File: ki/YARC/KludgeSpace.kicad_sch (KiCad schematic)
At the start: 5 parts, among them J8 6-PIN FROM MCR, U100 74LS32, U101 74LS157, U139 74HC74, U140 74LS32

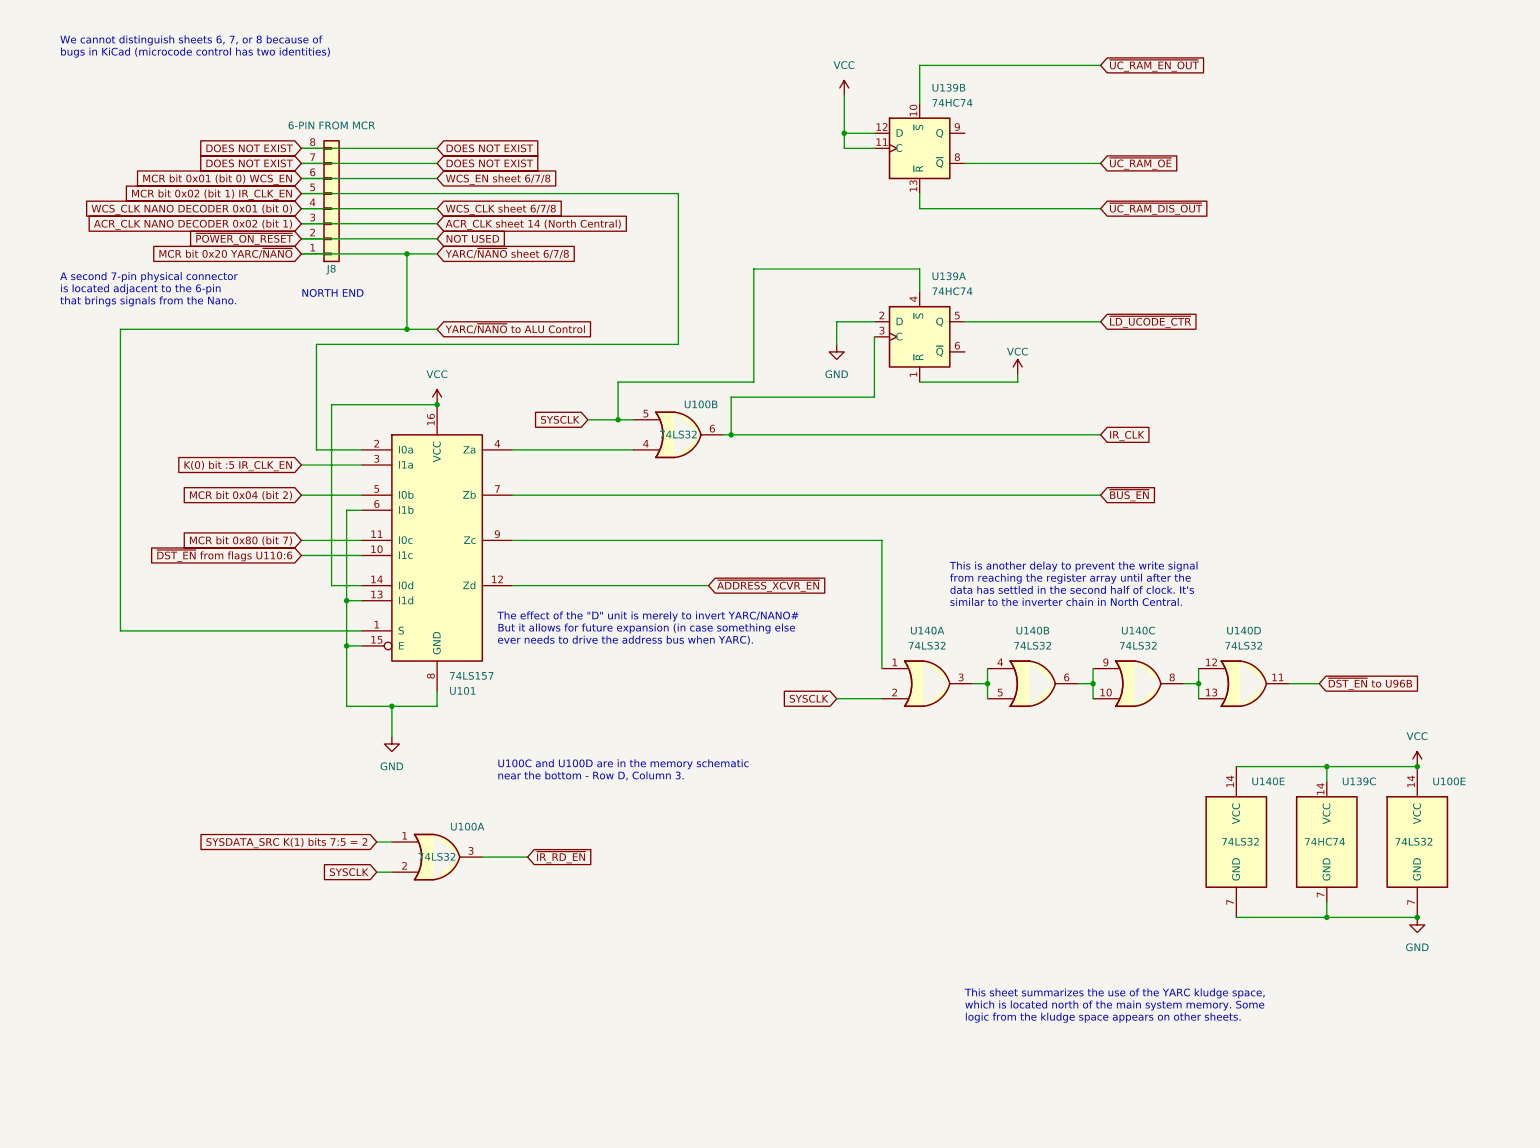
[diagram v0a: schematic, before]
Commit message: Ongoing fixes for ERC errors
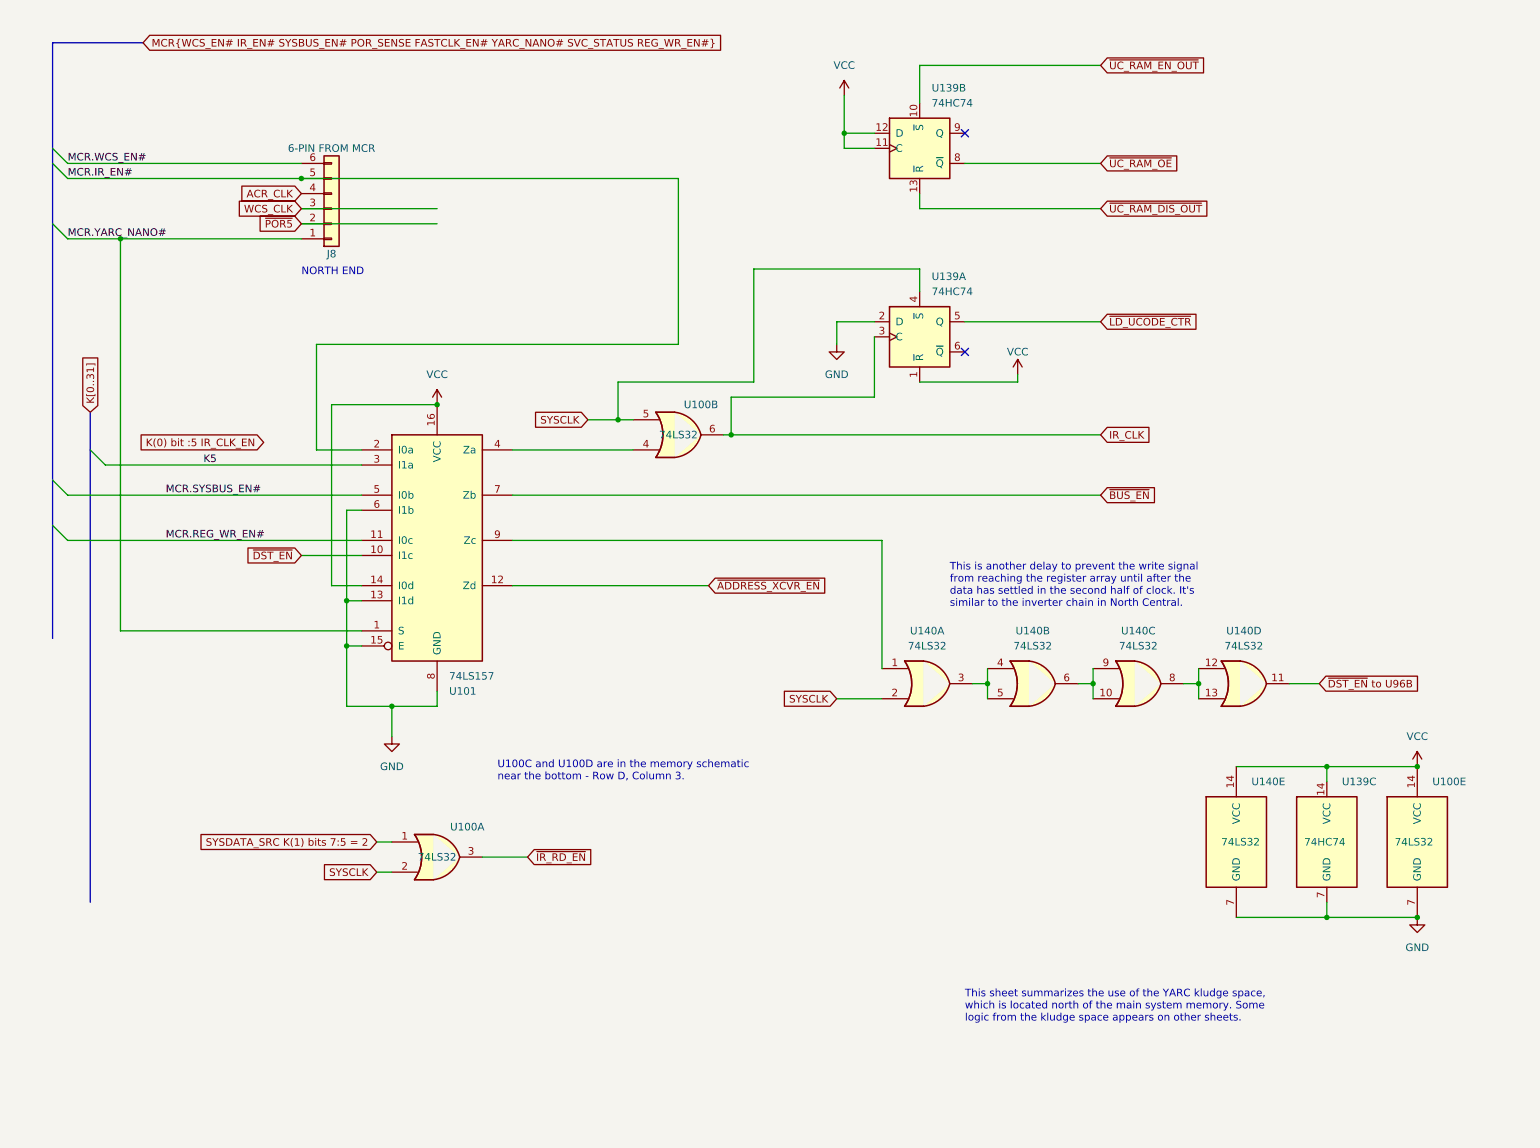
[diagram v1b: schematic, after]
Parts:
- J8: symbol Connector_Generic:Conn_01x08 -> Connector_Generic:Conn_01x06
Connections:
- net K(0) bit :5 IR_CLK_EN: no longer U101.3 (I1a)
- net ACR_CLK NANO DECODER 0x02 (bit 1) renamed WCS_CLK
- removed net DOES NOT EXIST: J8.7 (Pin_7), J8.8 (Pin_8)
- net MCR bit 0x01 (bit 0) WCS_EN renamed MCR.WCS_EN#
- net MCR bit 0x02 (bit 1) IR_CLK_EN renamed MCR.IR_EN#
- net MCR bit 0x04 (bit 2) renamed MCR.SYSBUS_EN#
- net MCR bit 0x20 YARC/~{NANO} renamed MCR.YARC_NANO#
- net MCR bit 0x80 (bit 7) renamed MCR.REG_WR_EN#
- net NOT USED renamed ~{POR5}
- net WCS_CLK NANO DECODER 0x01 (bit 0) renamed ACR_CLK
- net ~{DST_EN} from flags U110:6 renamed ~{DST_EN}
- new net K5: U101.3 (I1a)
- no-connect marks 0 -> 2
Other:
- note removed: "A second 7-pin physical connector is located adjacent to the 6-pin that brings signals from the Nano."
- note removed: "The effect of the "D" unit is merely to invert YARC/NANO# But it allows for future expansion (in case something else ever needs to drive the address bus when YARC)."
- note removed: "We cannot distinguish sheets 6, 7, or 8 because of bugs in KiCad (microcode control has two identities)"

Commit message: Ongoing schematic changes
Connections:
- net SYSDATA_SRC K(1) bits 7:5 = 2 renamed ~{SYSDATA_SRC_IS_IR}
- net ~{ADDRESS_XCVR_EN} renamed ~{GRtoA}
- net ~{DST_EN} to U96B renamed ~{DST_EN_DLY}
- net ~{IR_RD_EN} renamed ~{IR_RD}
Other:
- note added: "Delay the load of the microcode counter by 1/2 clock."
- note added: "Delay to prevent the write signal from reaching the register array until after the data has settled in the second half of clock. Similar to the inverter chain in North Central."
- note added: "Enable data output from the microcode RAMs from the Nano's pulse outputs."
- note added: "To U96B on p.10, GeneralRegisters"
- note added: "U100C and U100D are on the memory schematic."
- note removed: "This is another delay to prevent the write signal from reaching the register array until after the data has settled in the second half of clock. It's similar to the inverter chain in North Central."
- note removed: "U100C and U100D are in the memory schematic near the bottom - Row D, Column 3."
- moved on the sheet: J8, U100A, U100E, U101, U139A, U139B, U139C, U140A, U140B, U140C, U140D, U140E

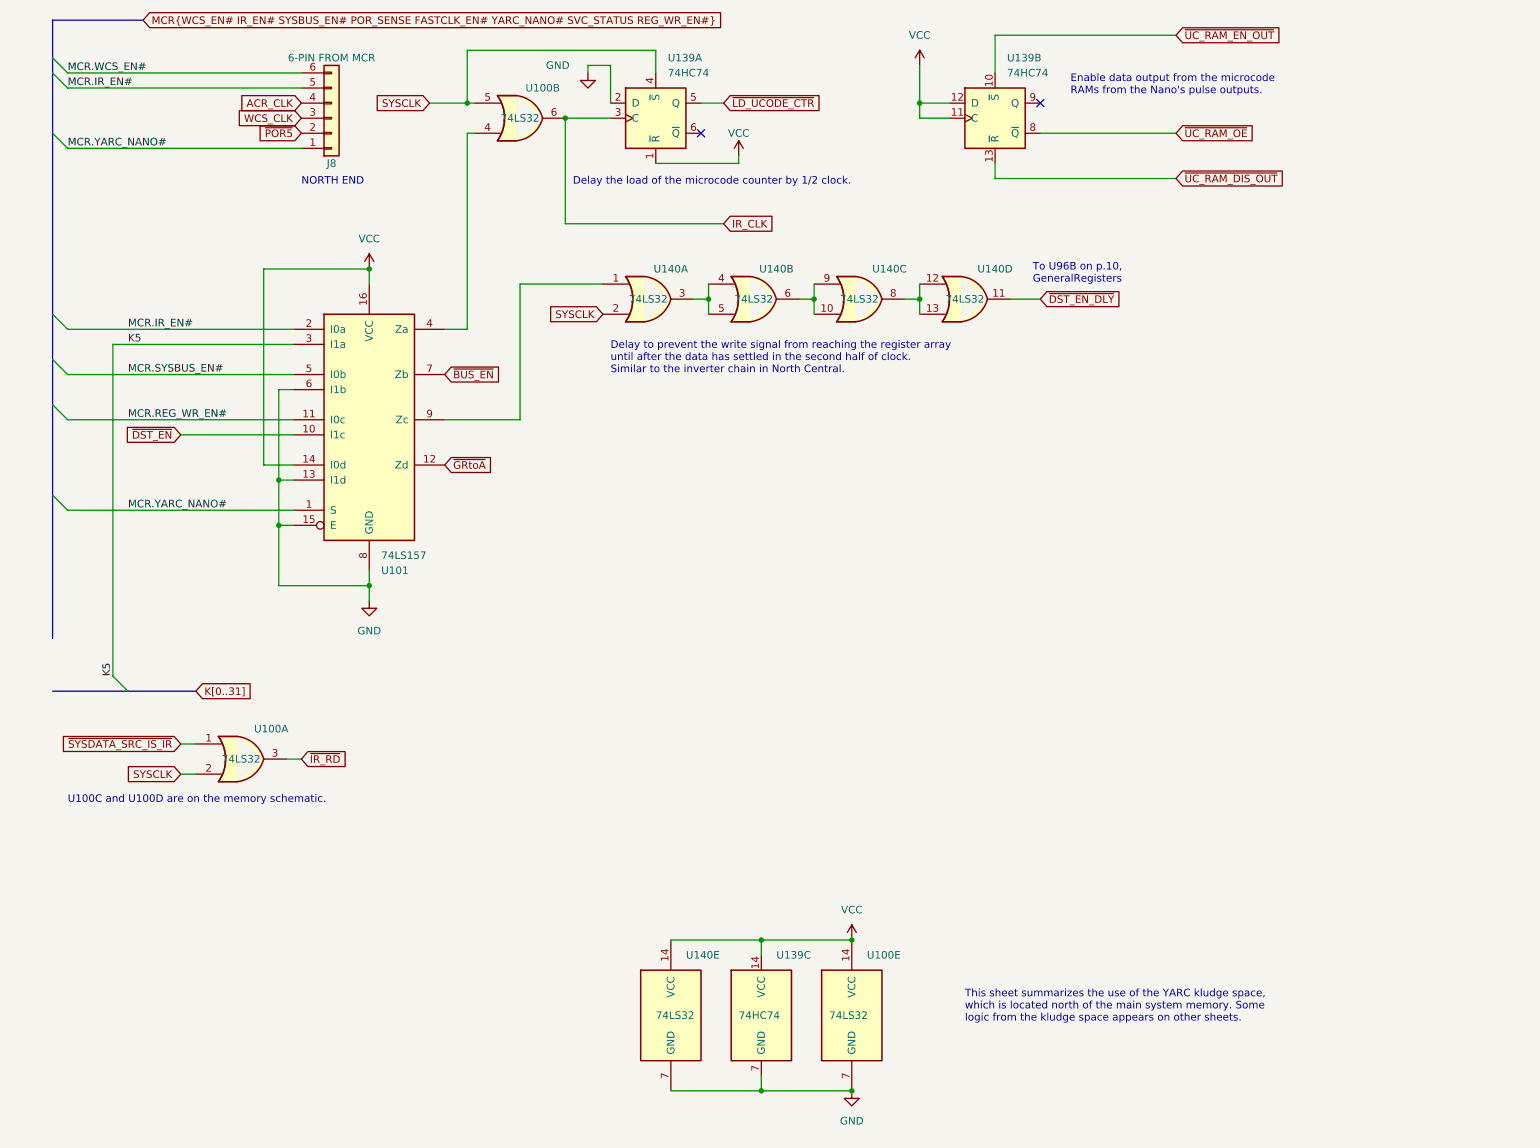
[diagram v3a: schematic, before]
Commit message: Schematic for addressing unit is complete and all ERC violations addressed
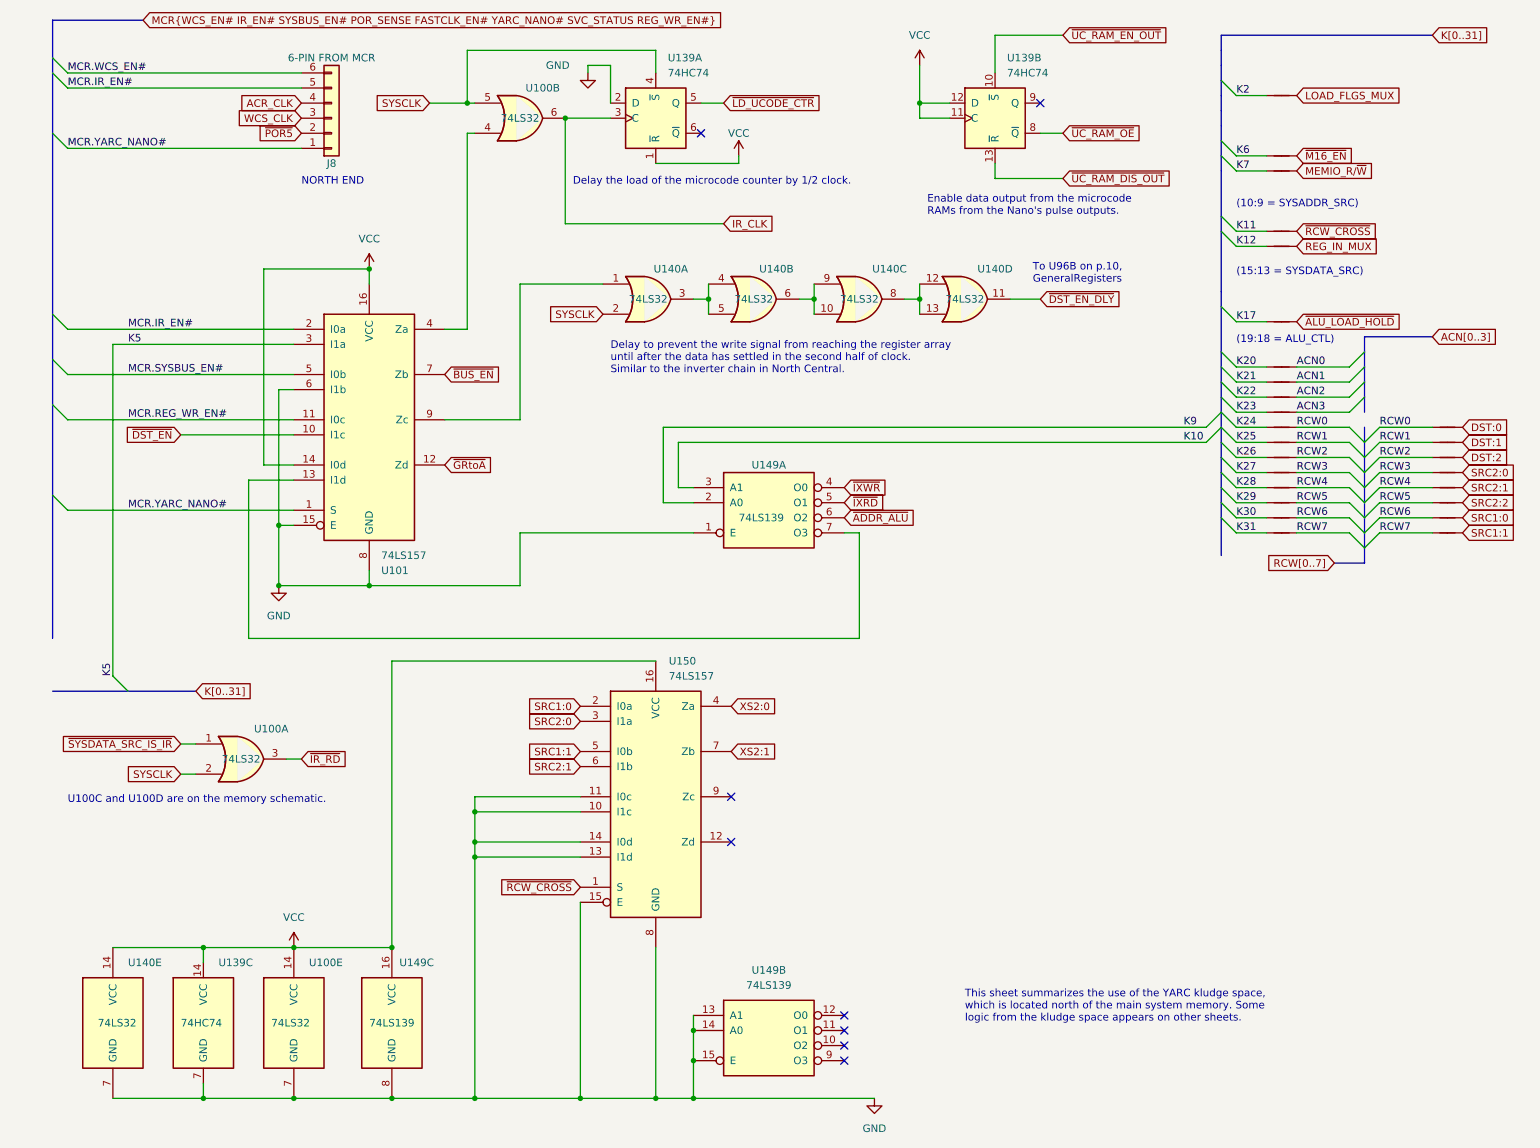
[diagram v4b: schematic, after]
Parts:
- added NT148, NT152, NT153, NT157, NT158, NT163, NT166, NT167, NT168, NT169, NT170, NT171, NT172, NT173, NT174, NT175, NT176, NT177, NT178, NT179, NT180, NT181, NT182, NT183, NT184, NT185: NetTie_2, symbol Device:NetTie_2
- added U149: 74LS139, symbol 74xx:74LS139
- added U150: 74LS157, symbol 74xx:74LS157
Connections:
- net GND: now also U149.1 (E), U149.13 (A1), U149.14 (A0), U149.15 (E), U149.8 (GND), U150.10 (I1c), U150.11 (I0c), U150.13 (I1d), U150.14 (I0d), U150.15 (E), U150.8 (GND); no longer U101.13 (I1d)
- net VCC: now also U149.16 (VCC), U150.16 (VCC)
- new net: U101.13 (I1d), U149.7 (O3)
- new net ACN0: NT166.2
- new net ACN1: NT167.2
- new net ACN2: NT168.2
- new net ACN3: NT169.2
- new net DST:0: NT178.2
- new net DST:1: NT179.2
- new net DST:2: NT180.2
- new net K10: U149.3 (A1)
- new net K11: NT157.1
- new net K12: NT158.1
- new net K17: NT163.1
- new net K2: NT148.1
- new net K20: NT166.1
- new net K21: NT167.1
- new net K22: NT168.1
- new net K23: NT169.1
- new net K24: NT170.1
- new net K25: NT171.1
- new net K26: NT172.1
- new net K27: NT173.1
- new net K28: NT174.1
- new net K29: NT175.1
- new net K30: NT176.1
- new net K31: NT177.1
- new net K6: NT152.1
- new net K7: NT153.1
- new net K9: U149.2 (A0)
- new net LOAD_FLGS_MUX: NT148.2
- new net MEMIO_R/~{W}: NT153.2
- new net RCW0: NT170.2, NT178.1
- new net RCW1: NT171.2, NT179.1
- new net RCW2: NT172.2, NT180.1
- new net RCW3: NT173.2, NT181.1
- new net RCW4: NT174.2, NT182.1
- new net RCW5: NT175.2, NT183.1
- new net RCW6: NT176.2, NT184.1
- new net RCW7: NT177.2, NT185.1
- new net REG_IN_MUX: NT158.2
- new net SRC1:0: NT184.2, U150.2 (I0a)
- new net SRC1:1: NT185.2, U150.5 (I0b)
- new net SRC2:0: NT181.2, U150.3 (I1a)
- new net SRC2:1: NT182.2, U150.6 (I1b)
- new net SRC2:2: NT183.2
- new net XS2:0: U150.4 (Za)
- new net XS2:1: U150.7 (Zb)
- new net ~{ADDR_ALU}: U149.6 (O2)
- new net ~{ALU_LOAD_HOLD}: NT163.2
- new net ~{IXRD}: U149.5 (O1)
- new net ~{IXWR}: U149.4 (O0)
- new net ~{M16_EN}: NT152.2
- new net ~{RCW_CROSS}: NT157.2, U150.1 (S)
- no-connect marks 2 -> 8
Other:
- note added: "(10:9 = SYSADDR_SRC)"
- note added: "(15:13 = SYSDATA_SRC)"
- note added: "(19:18 = ALU_CTL)"
- moved on the sheet: U100E, U139C, U140E
